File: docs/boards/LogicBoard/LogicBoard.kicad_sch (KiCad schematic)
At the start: 0 parts

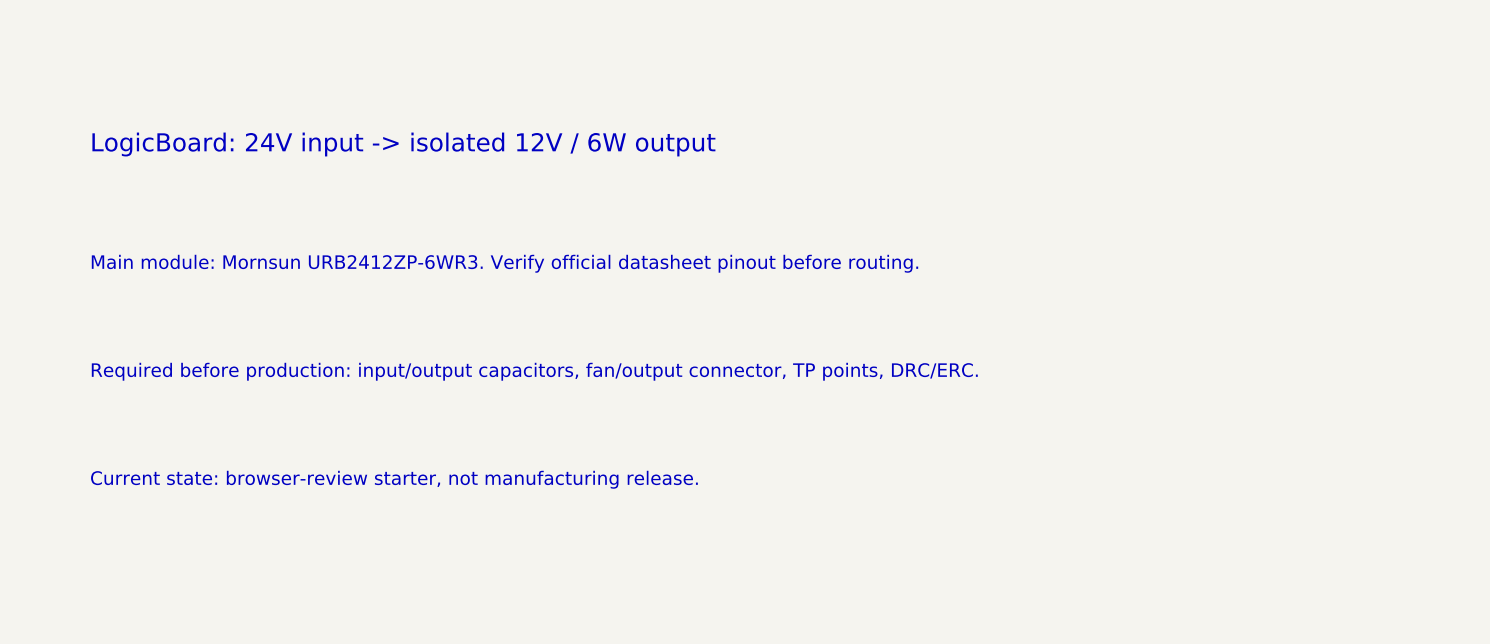
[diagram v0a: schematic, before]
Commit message: v4F generate real LogicBoard schematic from netlist lock
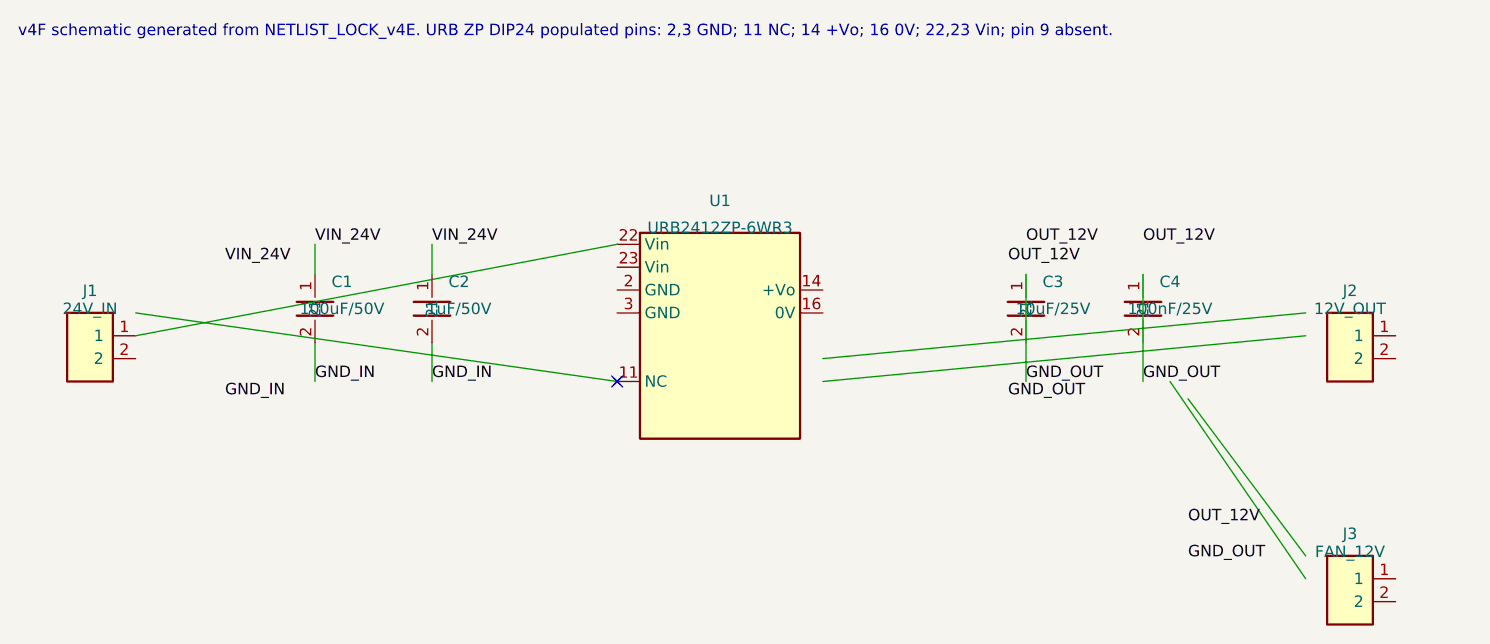
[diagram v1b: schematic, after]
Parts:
- added C1: 100uF/50V, CP_Radial, symbol Custom:CAP2
- added C2: 1uF/50V, C1206, symbol Custom:CAP2
- added C3: 10uF/25V, CP_Radial, symbol Custom:CAP2
- added C4: 100nF/25V, C1206, symbol Custom:CAP2
- added J1: 24V_IN, Terminal_2P_5_08, symbol Custom:CONN_2P
- added J2: 12V_OUT, Terminal_2P_5_08, symbol Custom:CONN_2P
- added J3: FAN_12V, Terminal_2P_5_08, symbol Custom:CONN_2P
- added U1: URB2412ZP-6WR3, Mornsun_URB2412ZP_6WR3_DIP24, symbol Custom:URB_ZP
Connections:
- new net: J1.1, U1.22 (Vin)
- new net GND_IN: C1.2, C2.2
- new net GND_OUT: C3.1, C4.1
- new net VIN_24V: C1.1, C2.1
- no-connect marks 0 -> 1
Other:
- note added: "v4F schematic generated from NETLIST_LOCK_v4E. URB ZP DIP24 populated pins: 2,3 GND; 11 NC; 14 +Vo; 16 0V; 22,23 Vin; pin 9 absent."
- note removed: "Current state: browser-review starter, not manufacturing release."
- note removed: "LogicBoard: 24V input -> isolated 12V / 6W output"
- note removed: "Main module: Mornsun URB2412ZP-6WR3. Verify official datasheet pinout before routing."
- note removed: "Required before production: input/output capacitors, fan/output connector, TP points, DRC/ERC."
- title: LogicBoard starter -> LogicBoard
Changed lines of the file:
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@@
 (kicad_sch (version 20230121) (generator "eeschema")
   (paper "A4")
-  (title_block (title "LogicBoard starter") (date "2026-06-14") (rev "v3-starter") (company "Docreate Mod"))
-  (text "LogicBoard: 24V input -> isolated 12V / 6W output" (at 20 25 0) (effects (font (size 2 2) (thickness 0.25)) (justify left bottom)))
-  (text "Main module: Mornsun URB2412ZP-6WR3. Verify official datasheet pinout before routing." (at 20 38 0) (effects (font (size 1.5 1.5) (thickness 0.2)) (justify left bottom)))
-  (text "Required before production: input/output capacitors, fan/output connector, TP points, DRC/ERC." (at 20 50 0) (effects (font (size 1.5 1.5) (thickness 0.2)) (justify left bottom)))
-  (text "Current state: browser-review starter, not manufacturing release." (at 20 62 0) (effects (font (size 1.5 1.5) (thickness 0.2)) (justify left bottom)))
+  (title_block (title "LogicBoard") (date "2026-06-14") (rev "v4F") (company "Docreate Mod"))
+  (text "v4F schematic generated from NETLIST_LOCK_v4E. URB ZP DIP24 populated pins: 2,3 GND; 11 NC; 14 +Vo; 16 0V; 22,23 Vin; pin 9 absent." (at 12 12 0) (effects (font (size 1.27 1.27) (thickness 0.18)) (justify left bottom)))
+  (symbol (lib_id "Custom:CONN_2P") (at 20 45 0) (unit 1) (in_bom yes) (on_board yes) (dnp no)
+    (property "Reference" "J1" (at 20 40 0) (effects (font (size 1.27 1.27))))
+    (property "Value" "24V_IN" (at 20 42 0) (effects (font (size 1.27 1.27))))
+    (property "Footprint" "Terminal_2P_5_08" (at 20 45 0) (effects (font (size 1.27 1.27)) hide))
+    (pin "1")
+    (pin "2")
+  )
+  (symbol (lib_id "Custom:CAP2") (at 45 42 0) (unit 1) (in_bom yes) (on_board yes) (dnp no)
+    (property "Reference" "C1" (at 48 39 0) (effects (font (size 1.27 1.27))))
+    (property "Value" "100uF/50V" (at 48 42 0) (effects (font (size 1.27 1.27))))
+    (property "Footprint" "CP_Radial" (at 45 42 0) (effects (font (size 1.27 1.27)) hide))
+    (pin "1")
+    (pin "2")
+  )
+  (symbol (lib_id "Custom:CAP2") (at 58 42 0) (unit 1) (in_bom yes) (on_board yes) (dnp no)
+    (property "Reference" "C2" (at 61 39 0) (effects (font (size 1.27 1.27))))
+    (property "Value" "1uF/50V" (at 61 42 0) (effects (font (size 1.27 1.27))))
+    (property "Footprint" "C1206" (at 58 42 0) (effects (font (size 1.27 1.27)) hide))
+    (pin "1")
+    (pin "2")
+  )
+  (symbol (lib_id "Custom:URB_ZP") (at 90 45 0) (unit 1) (in_bom yes) (on_board yes) (dnp no)
+    (property "Reference" "U1" (at 90 30 0) (effects (font (size 1.27 1.27))))
+    (property "Value" "URB2412ZP-6WR3" (at 90 33 0) (effects (font (size 1.27 1.27))))
+    (property "Footprint" "Mornsun_URB2412ZP_6WR3_DIP24" (at 90 45 0) (effects (font (size 1.27 1.27)) hide))
+    (pin "2")
+    (pin "3")
+    (pin "11")
+    (pin "14")
+    (pin "16")
+    (pin "22")
+    (pin "23")
+  )
+  (symbol (lib_id "Custom:CAP2") (at 124 42 0) (unit 1) (in_bom yes) (on_board yes) (dnp no)
+    (property "Reference" "C3" (at 127 39 0) (effects (font (size 1.27 1.27))))
+    (property "Value" "10uF/25V" (at 127 42 0) (effects (font (size 1.27 1.27))))
+    (property "Footprint" "CP_Radial" (at 124 42 0) (effects (font (size 1.27 1.27)) hide))
+    (pin "1")
+    (pin "2")
+  )
+  (symbol (lib_id "Custom:CAP2") (at 137 42 0) (unit 1) (in_bom yes) (on_board yes) (dnp no)
+    (property "Reference" "C4" (at 140 39 0) (effects (font (size 1.27 1.27))))
+    (property "Value" "100nF/25V" (at 140 42 0) (effects (font (size 1.27 1.27))))
+    (property "Footprint" "C1206" (at 137 42 0) (effects (font (size 1.27 1.27)) hide))
+    (pin "1")
+    (pin "2")
+  )
+  (symbol (lib_id "Custom:CONN_2P") (at 160 45 0) (unit 1) (in_bom yes) (on_board yes) (dnp no)
+    (property "Reference" "J2" (at 160 40 0) (effects (font (size 1.27 1.27))))
+    (property "Value" "12V_OUT" (at 160 42 0) (effects (font (size 1.27 1.27))))
+    (property "Footprint" "Terminal_2P_5_08" (at 160 45 0) (effects (font (size 1.27 1.27)) hide))
+    (pin "1")
+    (pin "2")
+  )
+  (symbol (lib_id "Custom:CONN_2P") (at 160 72 0) (unit 1) (in_bom yes) (on_board yes) (dnp no)
+    (property "Reference" "J3" (at 160 67 0) (effects (font (size 1.27 1.27))))
+    (property "Value" "FAN_12V" (at 160 69 0) (effects (font (size 1.27 1.27))))
+    (property "Footprint" "Terminal_2P_5_08" (at 160 72 0) (effects (font (size 1.27 1.27)) hide))
+    (pin "1")
+    (pin "2")
+  )
+  (wire (pts (xy 25.08 45) (xy 78.57 34.84)) (stroke (width 0) (type default)))
+  (label "VIN_24V" (at 35 37 0) (effects (font (size 1.27 1.27)) (justify left bottom)))
+  (wire (pts (xy 25.08 42.46) (xy 78.57 50.08)) (stroke (width 0) (type default)))
+  (label "GND_IN" (at 35 52 0) (effects (font (size 1.27 1.27)) (justify left bottom)))
+  (wire (pts (xy 45 38.19) (xy 45 34.84)) (stroke (width 0) (type default)))
+  (label "VIN_24V" (at 45 34.84 0) (effects (font (size 1.27 1.27)) (justify left bottom)))
+  (wire (pts (xy 45 45.81) (xy 45 50.08)) (stroke (width 0) (type default)))
+  (label "GND_IN" (at 45 50.08 0) (effects (font (size 1.27 1.27)) (justify left bottom)))
+  (wire (pts (xy 58 38.19) (xy 58 34.84)) (stroke (width 0) (type default)))
+  (label "VIN_24V" (at 58 34.84 0) (effects (font (size 1.27 1.27)) (justify left bottom)))
+  (wire (pts (xy 58 45.81) (xy 58 50.08)) (stroke (width 0) (type default)))
+  (label "GND_IN" (at 58 50.08 0) (effects (font (size 1.27 1.27)) (justify left bottom)))
+  (wire (pts (xy 101.43 50.08) (xy 155.08 45)) (stroke (width 0) (type default)))
+  (label "OUT_12V" (at 122 37 0) (effects (font (size 1.27 1.27)) (justify left bottom)))
+  (wire (pts (xy 101.43 47.54) (xy 155.08 42.46)) (stroke (width 0) (type default)))
+  (label "GND_OUT" (at 122 52 0) (effects (font (size 1.27 1.27)) (justify left bottom)))
+  (wire (pts (xy 124 38.19) (xy 124 50.08)) (stroke (width 0) (type default)))
+  (label "OUT_12V" (at 124 34.84 0) (effects (font (size 1.27 1.27)) (justify left bottom)))
+  (label "GND_OUT" (at 124 50.08 0) (effects (font (size 1.27 1.27)) (justify left bottom)))
+  (wire (pts (xy 137 38.19) (xy 137 50.08)) (stroke (width 0) (type default)))
+  (label "OUT_12V" (at 137 34.84 0) (effects (font (size 1.27 1.27)) (justify left bottom)))
+  (label "GND_OUT" (at 137 50.08 0) (effects (font (size 1.27 1.27)) (justify left bottom)))
+  (wire (pts (xy 155.08 72) (xy 140 50.08)) (stroke (width 0) (type default)))
+  (label "OUT_12V" (at 142 66 0) (effects (font (size 1.27 1.27)) (justify left bottom)))
+  (wire (pts (xy 155.08 69.46) (xy 142 52)) (stroke (width 0) (type default)))
+  (label "GND_OUT" (at 142 70 0) (effects (font (size 1.27 1.27)) (justify left bottom)))
+  (no_connect (at 78.57 50.08))
   (sheet_instances (path "/" (page "1")))
 )
